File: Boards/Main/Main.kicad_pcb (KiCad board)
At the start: 2 copper layers, 99 x 84.6 mm, 25 parts, among them J1 Power, J2 PWM 7-0, J3 Digital, J5 Conn_01x16, J6 Conn_01x16, Q1 16 MHz, SW1 RESET, U3 WD42C22, U4 6116 SRAM

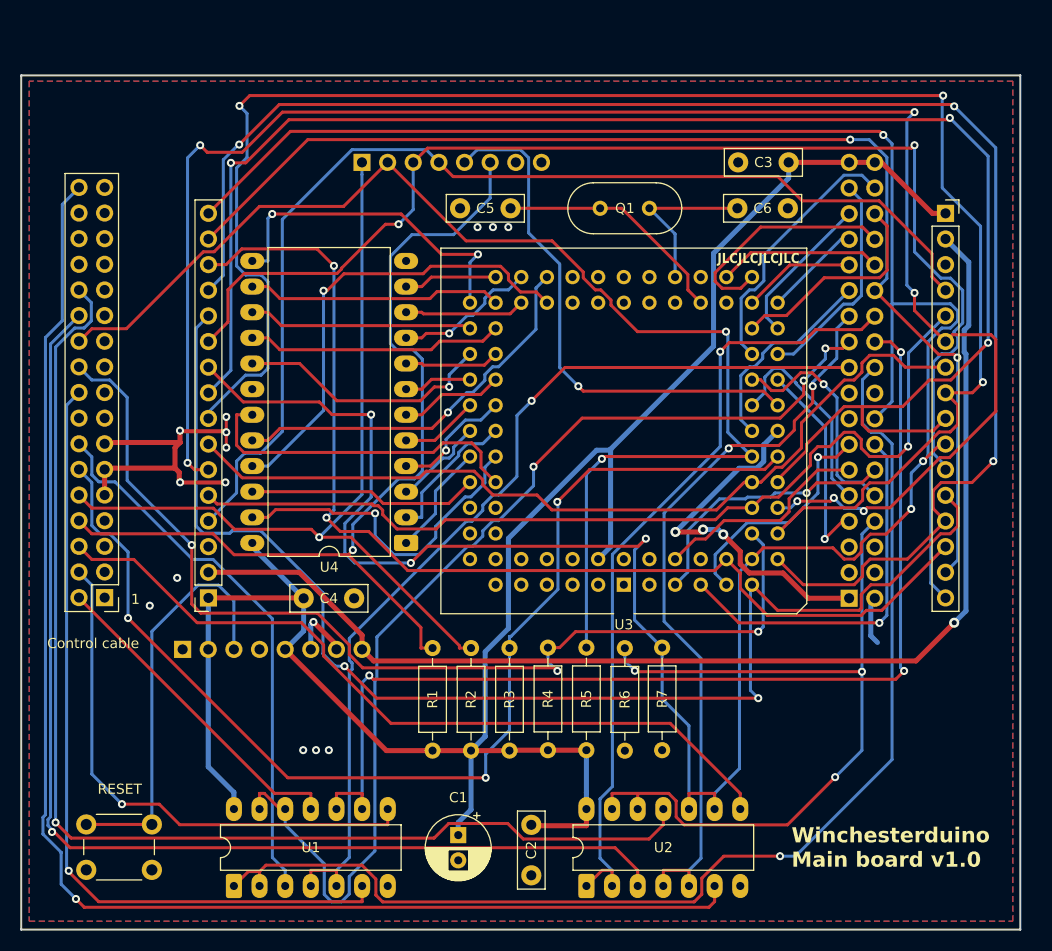
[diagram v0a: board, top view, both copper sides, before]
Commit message: v1.1 mainboard: add microSD card support, 32K buffer SRAM
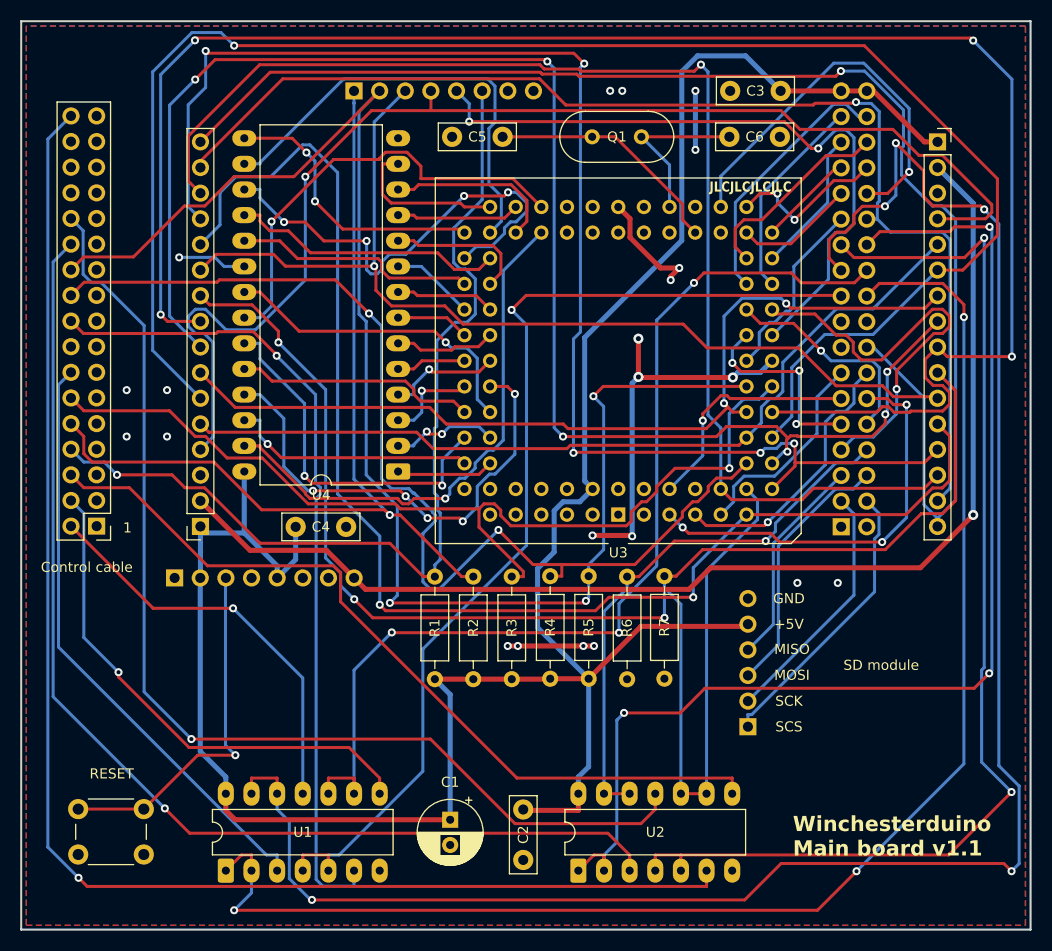
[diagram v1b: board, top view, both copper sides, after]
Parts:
- added J7: Digital, Connector_PinHeader_2.54mm:PinHeader_1x06_P2.54mm_Vertical, F.Cu at (179.8, 117.3)
- Q1: value 16 MHz -> 20 MHz
- U4: value 6116 SRAM -> 62256 SRAM; footprint Package_DIP:DIP-24_W15.24mm_LongPads -> Package_DIP:DIP-28_W15.24mm_LongPads
- moved C4 7.12 mm to (135.0, 97.5)
- moved J6 7.12 mm to (198.6, 59.4)
- moved J1 7.12 mm to (123.0, 102.6)
- moved J4 7.12 mm to (115.3, 97.4)
- moved C6 7.12 mm to (183.0, 58.8)
- moved Q1 7.12 mm to (164.4, 58.8)
- moved C3 7.12 mm to (183.1, 54.3)
- moved C5 7.12 mm to (150.5, 58.8)
- moved J2 7.12 mm to (140.8, 54.3)
- moved J3 7.12 mm to (189.1, 97.5)
- moved J5 7.12 mm to (125.6, 97.5)
- moved U4 7.12 mm to (145.2, 92.0)
- moved R1 7.08 mm to (148.8, 112.6)
- moved R2 7.08 mm to (152.6, 112.6)
- moved R3 7.08 mm to (156.4, 112.6)
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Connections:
- J3 pad 3: unconnected-(J3-Pin_3-Pad3) -> /SCK
- J3 pad 4: unconnected-(J3-Pin_4-Pad4) -> /SCS
- J3 pad 5: unconnected-(J3-Pin_5-Pad5) -> /MISO
- J3 pad 6: unconnected-(J3-Pin_6-Pad6) -> /MOSI
- U3 pad 70: unconnected-(U3-BA11-Pad70) -> /BA11
- U3 pad 71: unconnected-(U3-BA12-Pad71) -> /BA12
- U3 pad 72: unconnected-(U3-BA13-Pad72) -> /BA13
- U3 pad 73: unconnected-(U3-BA14-Pad73) -> /BA14
- U4 pad 1: /BA7 -> /BA14
- U4 pad 10: /BD1 -> /BA0
- U4 pad 11: /BD2 -> /BD0
- U4 pad 12: GND -> /BD1
- U4 pad 13: /BD3 -> /BD2
- U4 pad 14: /BD4 -> GND
- U4 pad 15: /BD5 -> /BD3
- U4 pad 16: /BD6 -> /BD4
- U4 pad 17: /BD7 -> /BD5
- U4 pad 18: GND -> /BD6
- U4 pad 19: /BA10 -> /BD7
- U4 pad 2: /BA6 -> /BA12
- U4 pad 20: /~{BOE} -> GND
- U4 pad 21: /~{BWE} -> /BA10
- U4 pad 22: /BA9 -> /~{BOE}
- U4 pad 23: /BA8 -> /BA11
- U4 pad 24: +5V -> /BA9
- U4 pad 3: /BA5 -> /BA7
- U4 pad 4: /BA4 -> /BA6
- U4 pad 5: /BA3 -> /BA5
- U4 pad 6: /BA2 -> /BA4
- U4 pad 7: /BA1 -> /BA3
- U4 pad 8: /BA0 -> /BA2
- U4 pad 9: /BD0 -> /BA1
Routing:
- net /HDSEL3: track 106.2 -> 186.8 mm, vias 3 -> 5
- net /DIR: track 74.4 -> 112.7 mm
- net +5V: track 201.8 -> 239.9 mm
- net /STEP: track 79.9 -> 116.3 mm, vias 1 -> 3
- net /BA11: track 0.00 -> 36.2 mm, vias 0 -> 2
- net /SCS: track 0.00 -> 28.5 mm
- net /DS: track 81.6 -> 54.4 mm, vias 3 -> 1
- net /HDSEL0: track 117.8 -> 144.2 mm, vias 1 -> 3
- net /MOSI: track 0.00 -> 25.7 mm
- net /BD5: track 22.2 -> 47.1 mm, vias 0 -> 4
- net /SCK: track 0.00 -> 24.7 mm
- net /BA13: track 0.00 -> 24.5 mm, vias 0 -> 1
- net /AD7: track 16.2 -> 39.6 mm, vias 0 -> 1
- net /WGATE: track 152.9 -> 176.2 mm, vias 5 -> 3
- net /MISO: track 0.00 -> 21.1 mm
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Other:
- board size 99 x 84.6 mm -> 100 x 90 mm
- board text added: "+5V"
- board text added: "GND"
- board text added: "MISO"
- board text added: "MOSI"
- board text added: "SCK"
- board text added: "SCS"
- board text added: "SD module"
- board text added: "Winchesterduino Main board v1.1"
- board text removed: "Winchesterduino Main board v1.0"
